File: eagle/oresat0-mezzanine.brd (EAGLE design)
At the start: 80 x 74 mm, 22 parts, among them U1 QBA-07+, U2 QBA-07+, U3 QBA-07+, U7 QCN-XXX+, U8 QCN-XXX+, U9 QCN-XXX+

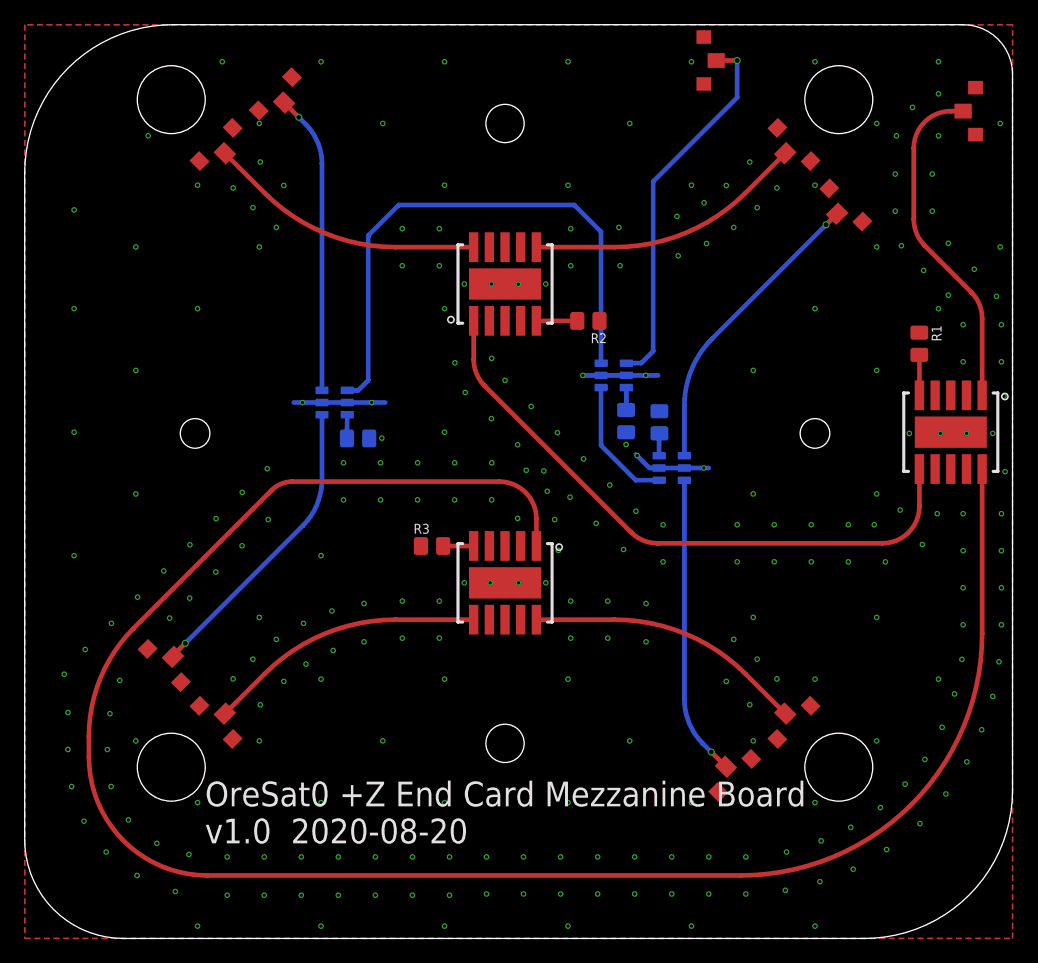
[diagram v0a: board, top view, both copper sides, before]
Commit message: Final cleanup and polish of v1.1 OreSat0 +Z end card and mezzanine. Fixed S band 1/4 wave, lots of stiching and polish, fixed radial TCREAM on the contact pads, lots of TNAMES polish.
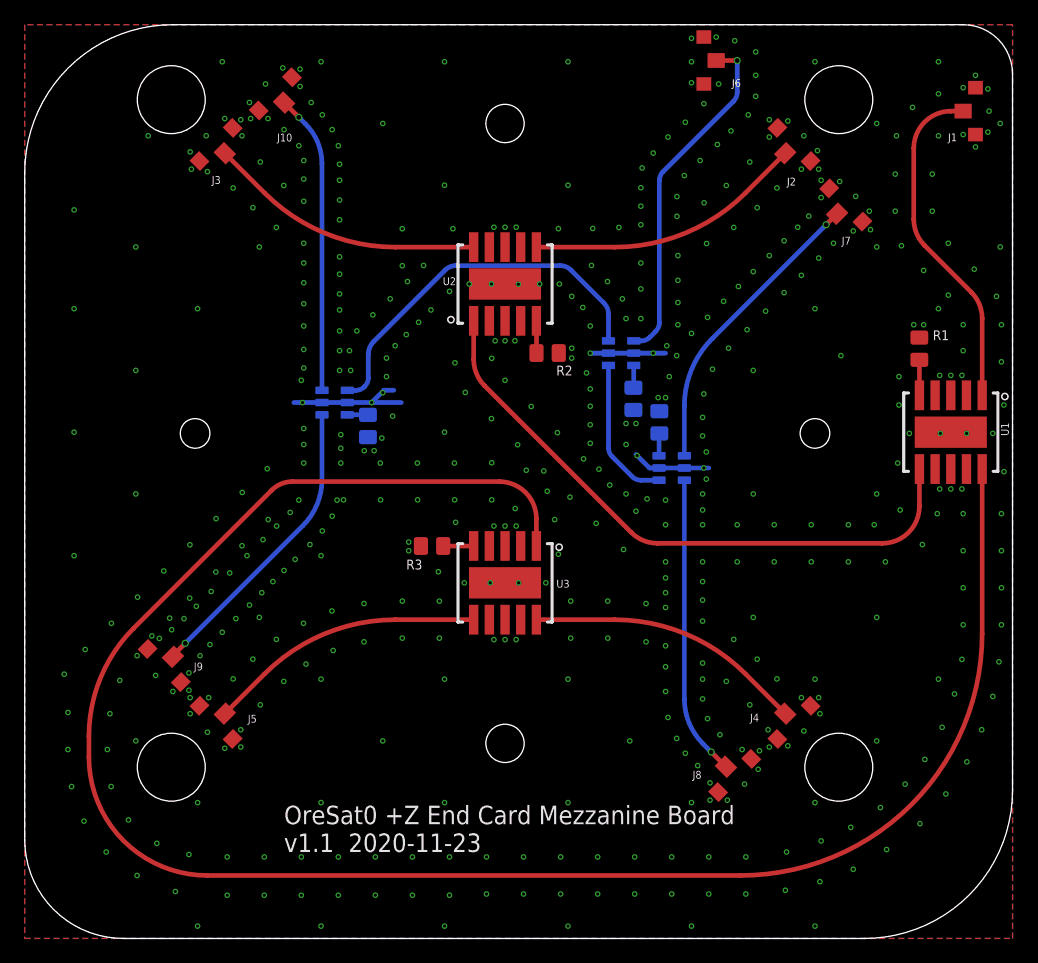
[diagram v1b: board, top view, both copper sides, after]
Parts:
- removed U$1, U$10, U$2, U$3, U$4, U$5, U$6, U$7, U$8, U$9: R107064070, J-Radiall-R107064070-RF:R107064070
- added J1, J10, J2, J3, J4, J5, J6, J7, J8, J9: R107064070, J-Radiall-R107064070-RF:R107064070_SOLDER
- moved R2 4.20 mm to (53.4, 56.3)
- moved R4 1.90 mm to (60.3, 52.6)
- moved U7 1.90 mm to (59.3, 56.3)
- moved R6 1.28 mm to (38.8, 50.4), turned to 90 degrees
- moved R1 0.40 mm to (83.5, 56.7)
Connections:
- net SBAND-1/4L renamed SBAND-SHORT+1/4WAVE
- net GND: now also J1.P$2, J1.P$3, J10.P$2, J10.P$3, J2.P$2, J2.P$3, J3.P$2, J3.P$3, J4.P$2, J4.P$3, J5.P$2, J5.P$3, J6.P$2, J6.P$3, J7.P$2, J7.P$3, J8.P$2, J8.P$3, J9.P$2, J9.P$3; no longer U$1.P$2, U$1.P$3, U$10.P$2, U$10.P$3, U$2.P$2, U$2.P$3, U$3.P$2, U$3.P$3, U$4.P$2, U$4.P$3, U$5.P$2, U$5.P$3, U$6.P$2, U$6.P$3, U$7.P$2, U$7.P$3, U$8.P$2, U$8.P$3, U$9.P$2, U$9.P$3
- net SBAND: now also J6.P$1; no longer U$6.P$1
- net SBAND_0: now also J7.P$1; no longer U$7.P$1
- net SBAND_180: now also J9.P$1; no longer U$9.P$1
- net SBAND_270: now also J10.P$1; no longer U$10.P$1
- net SBAND_90: now also J8.P$1; no longer U$8.P$1
- net UHF: now also J1.P$1; no longer U$1.P$1
- net UHF_0: now also J2.P$1; no longer U$2.P$1
- net UHF_180: now also J5.P$1; no longer U$4.P$1
- net UHF_270: now also J4.P$1; no longer U$5.P$1
- net UHF_90: now also J3.P$1; no longer U$3.P$1
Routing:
- net SBAND-SHORT+1/4WAVE: track 45.2 -> 30.7 mm
- net GND: track 19.9 -> 23.4 mm, vias 282 -> 534
- net SBAND: track 30.6 -> 28.2 mm
- net SBAND-SHORT: track 10.6 -> 12.0 mm
- net N$4: track 3.31 -> 2.61 mm
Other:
- board text added: "OreSat0 +Z End Card Mezzanine Board v1.1 2020-11-23"
- board text removed: "OreSat0 +Z End Card Mezzanine Board v1.0 2020-08-20"
- board text removed: "OreSat0 +Z End Card Mezzanine Board v1.1 2020-11-22"

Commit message: Clean up BOM and part numbers. Ready for v1.1 fab.
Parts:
- U7, U8, U9: value QCN-XXX+ -> QCN-27+
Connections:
- net UHF-1/4L renamed UHF-SHORT+1/4WAVE

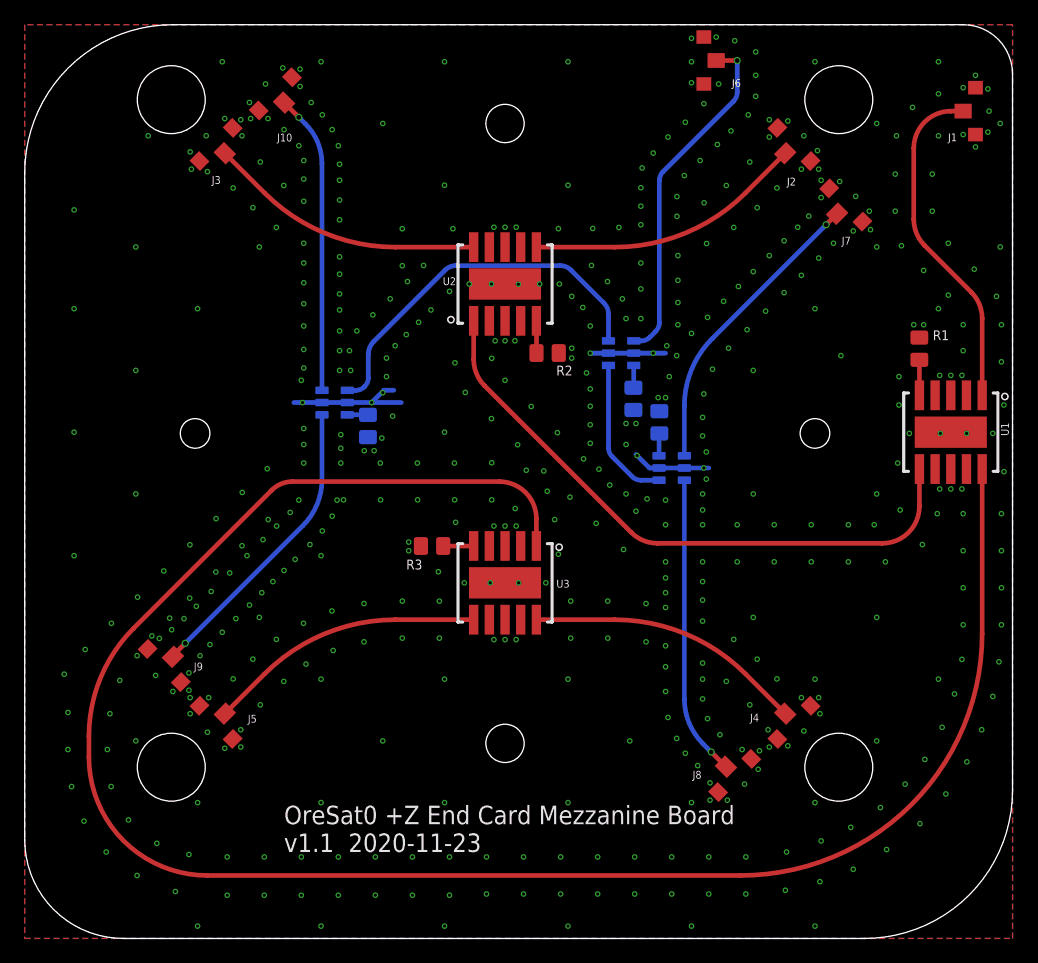
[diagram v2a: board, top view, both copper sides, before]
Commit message: Switched to a QCN-27D+ (with DC passthrough) for S band, and made the U and L band 1/4 wave lengths a bit more precise after getting precise lengths from Eric.
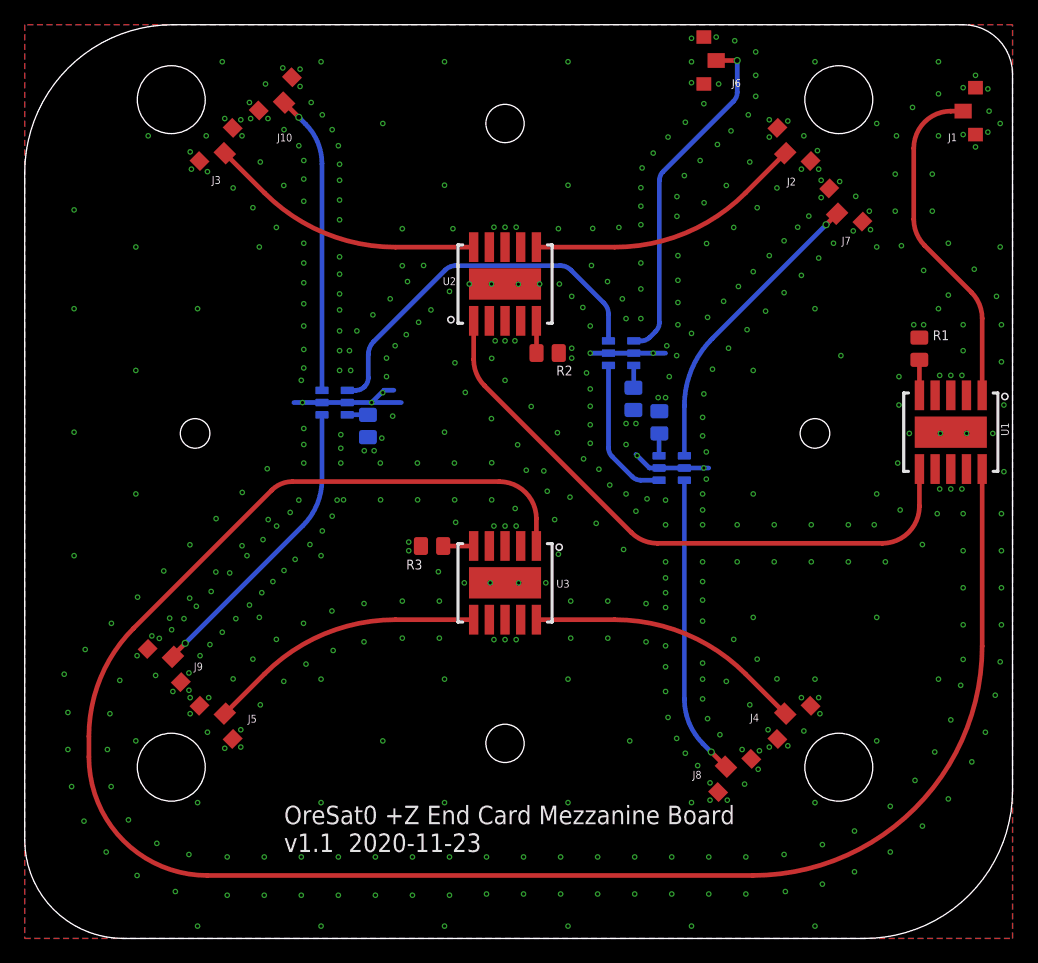
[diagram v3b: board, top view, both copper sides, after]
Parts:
- U7, U8, U9: value QCN-27+ -> QCN-27D+
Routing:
- net UHF-SHORT+1/4WAVE: track 149.8 -> 150.3 mm
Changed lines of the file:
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@@
 <wire x1="60.121321875" y1="41.778678125" x2="48.238678125" y2="53.661321875" width="2" layer="29"/>
 <wire x1="48.238678125" y1="53.661321875" x2="47.36" y2="56.382640625" width="2" layer="29" curve="-44.99994"/>
-<wire x1="88.54" y1="44.395" x2="88.54" y2="33.48" width="2" layer="29"/>
-<wire x1="88.54" y1="33.48" x2="68.96" y2="14" width="2" layer="29" curve="-90"/>
-<wire x1="68.96" y1="14" x2="25.79" y2="14" width="2" layer="29"/>
+<wire x1="88.54" y1="44.395" x2="88.54" y2="32.68" width="2" layer="29"/>
+<wire x1="88.54" y1="32.68" x2="69.96" y2="14" width="2" layer="29" curve="-90"/>
+<wire x1="69.96" y1="14" x2="25.79" y2="14" width="2" layer="29"/>
 <wire x1="25.79" y1="14" x2="16.1" y2="23.99" width="2" layer="29" curve="-90"/>
 <wire x1="16.1" y1="23.99" x2="16.2" y2="22.557359375" width="2" layer="29"/>
@@
 <attribute name="P-NP" value="P" x="31.3" y="77.3" size="1.778" layer="27" rot="R45" display="off"/>
 </element>
-<element name="U7" library="U-MiniCirc-QCN-XXX+-quad" package="QCN-XXX+" value="QCN-27+" x="59.3" y="56.3" smashed="yes" rot="MR270">
+<element name="U7" library="U-MiniCirc-QCN-XXX+-quad" package="QCN-XXX+" value="QCN-27D+" x="59.3" y="56.3" smashed="yes" rot="MR270">
 <attribute name="DESCRIPTION" value="Signal Conditioning LTCC 90 Hybrid, 1100-1925 MHz, 50 ohms" x="59.3" y="56.3" size="1.778" layer="28" rot="MR270" display="off"/>
 <attribute name="DIST" value="Mouser" x="59.3" y="56.3" size="1.778" layer="28" rot="MR270" display="off"/>
@@
 <attribute name="VALUE" x="60.7" y="53" size="0.6096" layer="28" font="vector" ratio="15" rot="MR0"/>
 </element>
-<element name="U8" library="U-MiniCirc-QCN-XXX+-quad" package="QCN-XXX+" value="QCN-27+" x="63.4" y="47" smashed="yes" rot="MR90">
+<element name="U8" library="U-MiniCirc-QCN-XXX+-quad" package="QCN-XXX+" value="QCN-27D+" x="63.4" y="47" smashed="yes" rot="MR90">
 <attribute name="DESCRIPTION" value="Signal Conditioning LTCC 90 Hybrid, 1100-1925 MHz, 50 ohms" x="63.4" y="47" size="1.778" layer="28" rot="MR90" display="off"/>
 <attribute name="DIST" value="Mouser" x="63.4" y="47" size="1.778" layer="28" rot="MR90" display="off"/>
@@
 <attribute name="VALUE" x="62" y="50.3" size="0.6096" layer="28" font="vector" ratio="15" rot="MR180"/>
 </element>
-<element name="U9" library="U-MiniCirc-QCN-XXX+-quad" package="QCN-XXX+" value="QCN-27+" x="36.1" y="52.3" smashed="yes" rot="MR270">
+<element name="U9" library="U-MiniCirc-QCN-XXX+-quad" package="QCN-XXX+" value="QCN-27D+" x="36.1" y="52.3" smashed="yes" rot="MR270">
 <attribute name="DESCRIPTION" value="Signal Conditioning LTCC 90 Hybrid, 1100-1925 MHz, 50 ohms" x="36.1" y="52.3" size="1.778" layer="28" rot="MR270" display="off"/>
 <attribute name="DIST" value="Mouser" x="36.1" y="52.3" size="1.778" layer="28" rot="MR270" display="off"/>
@@
 <via x="90.1" y="37.3" extent="1-16" drill="0.254"/>
 <via x="90.1" y="34.3" extent="1-16" drill="0.254"/>
-<via x="89.9" y="31.3" extent="1-16" drill="0.254"/>
-<via x="89.4" y="28.5" extent="1-16" drill="0.254"/>
-<via x="88.5" y="25.8" extent="1-16" drill="0.254"/>
-<via x="87.3" y="23.2" extent="1-16" drill="0.254"/>
-<via x="85.6" y="20.6" extent="1-16" drill="0.254"/>
-<via x="83.5" y="18.2" extent="1-16" drill="0.254"/>
-<via x="80.8" y="16.1" extent="1-16" drill="0.254"/>
-<via x="78.1" y="14.5" extent="1-16" drill="0.254"/>
-<via x="75.4" y="13.5" extent="1-16" drill="0.254"/>
-<via x="72.6" y="12.8" extent="1-16" drill="0.254"/>
+<via x="90" y="31.3" extent="1-16" drill="0.254"/>
+<via x="89.6" y="28.6" extent="1-16" drill="0.254"/>
+<via x="88.8" y="25.6" extent="1-16" drill="0.254"/>
+<via x="87.7" y="23.2" extent="1-16" drill="0.254"/>
+<via x="85.8" y="20.2" extent="1-16" drill="0.254"/>
+<via x="83.7" y="18" extent="1-16" drill="0.254"/>
+<via x="81.1" y="15.9" extent="1-16" drill="0.254"/>
+<via x="78.2" y="14.3" extent="1-16" drill="0.254"/>
+<via x="75.6" y="13.3" extent="1-16" drill="0.254"/>
+<via x="72.6" y="12.7" extent="1-16" drill="0.254"/>
 <via x="69.4" y="12.5" extent="1-16" drill="0.254"/>
 <via x="66.4" y="12.5" extent="1-16" drill="0.254"/>
 <via x="66.4" y="15.5" extent="1-16" drill="0.254"/>
 <via x="69.4" y="15.5" extent="1-16" drill="0.254"/>
-<via x="72.7" y="15.9" extent="1-16" drill="0.254"/>
-<via x="75.5" y="16.8" extent="1-16" drill="0.254"/>
-<via x="77.9" y="17.9" extent="1-16" drill="0.254"/>
-<via x="80.3" y="19.5" extent="1-16" drill="0.254"/>
-<via x="82.3" y="21.4" extent="1-16" drill="0.254"/>
-<via x="83.9" y="23.4" extent="1-16" drill="0.254"/>
-<via x="85.3" y="26" extent="1-16" drill="0.254"/>
-<via x="86.3" y="28.7" extent="1-16" drill="0.254"/>
-<via x="86.9" y="31.5" extent="1-16" drill="0.254"/>
+<via x="72.5" y="15.7" extent="1-16" drill="0.254"/>
+<via x="75.6" y="16.5" extent="1-16" drill="0.254"/>
+<via x="78.2" y="17.6" extent="1-16" drill="0.254"/>
+<via x="81.1" y="19.6" extent="1-16" drill="0.254"/>
+<via x="83.1" y="21.7" extent="1-16" drill="0.254"/>
+<via x="84.7" y="24" extent="1-16" drill="0.254"/>
+<via x="86" y="26.6" extent="1-16" drill="0.254"/>
+<via x="86.8" y="29.4" extent="1-16" drill="0.254"/>
+<via x="87" y="31.5" extent="1-16" drill="0.254"/>
 <via x="63.4" y="12.5" extent="1-16" drill="0.254"/>
 <via x="60.4" y="12.5" extent="1-16" drill="0.254"/>
@@
 <contactref element="U3" pad="1"/>
 <contactref element="U1" pad="10"/>
-<wire x1="88.54" y1="46.915" x2="88.54" y2="33.58" width="0.38" layer="1"/>
-<wire x1="88.54" y1="33.58" x2="68.96" y2="14" width="0.38" layer="1" curve="-90"/>
-<wire x1="68.96" y1="14" x2="25.79" y2="14" width="0.38" layer="1"/>
+<wire x1="88.54" y1="46.915" x2="88.54" y2="32.58" width="0.38" layer="1"/>
+<wire x1="88.54" y1="32.58" x2="69.96" y2="14" width="0.38" layer="1" curve="-90"/>
+<wire x1="69.96" y1="14" x2="25.79" y2="14" width="0.38" layer="1"/>
 <wire x1="25.79" y1="14" x2="16.2" y2="23.59" width="0.38" layer="1" curve="-90"/>
 <wire x1="16.2" y1="23.59" x2="16.2" y2="25.271571875" width="0.38" layer="1"/>
